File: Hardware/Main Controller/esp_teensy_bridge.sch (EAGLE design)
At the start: 4 parts, among them IC1 BQ79600PWRQ1

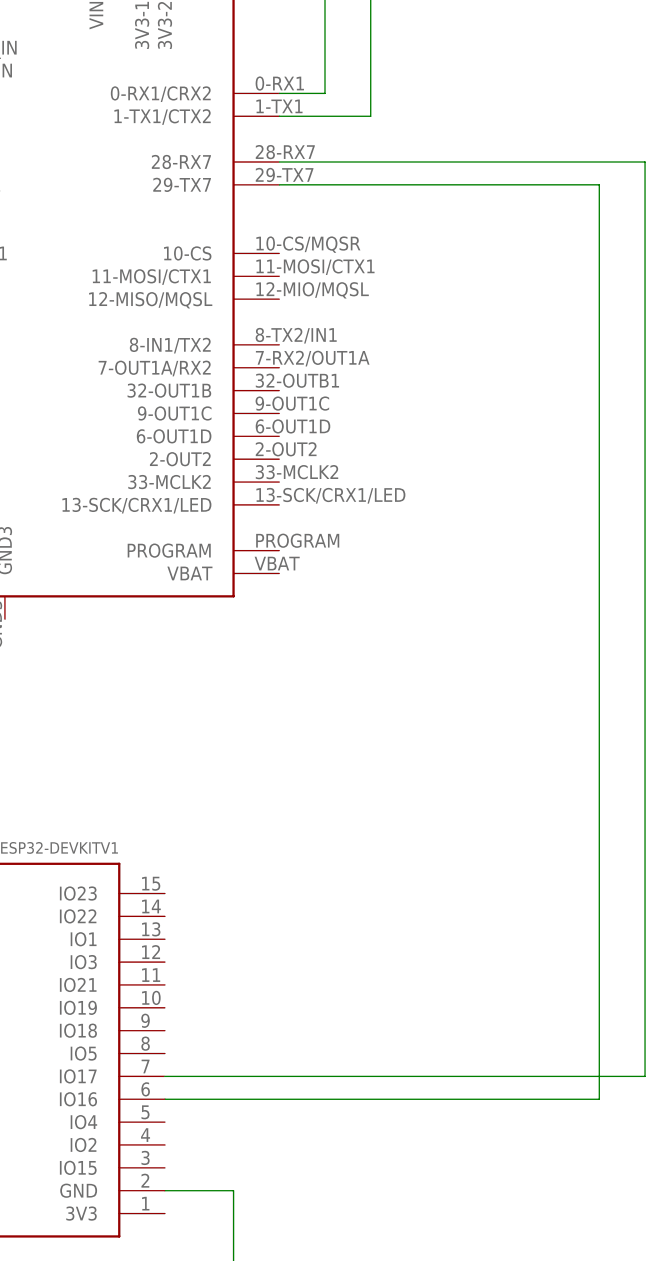
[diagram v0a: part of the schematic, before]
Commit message: Update esp_teensy_bridge.sch
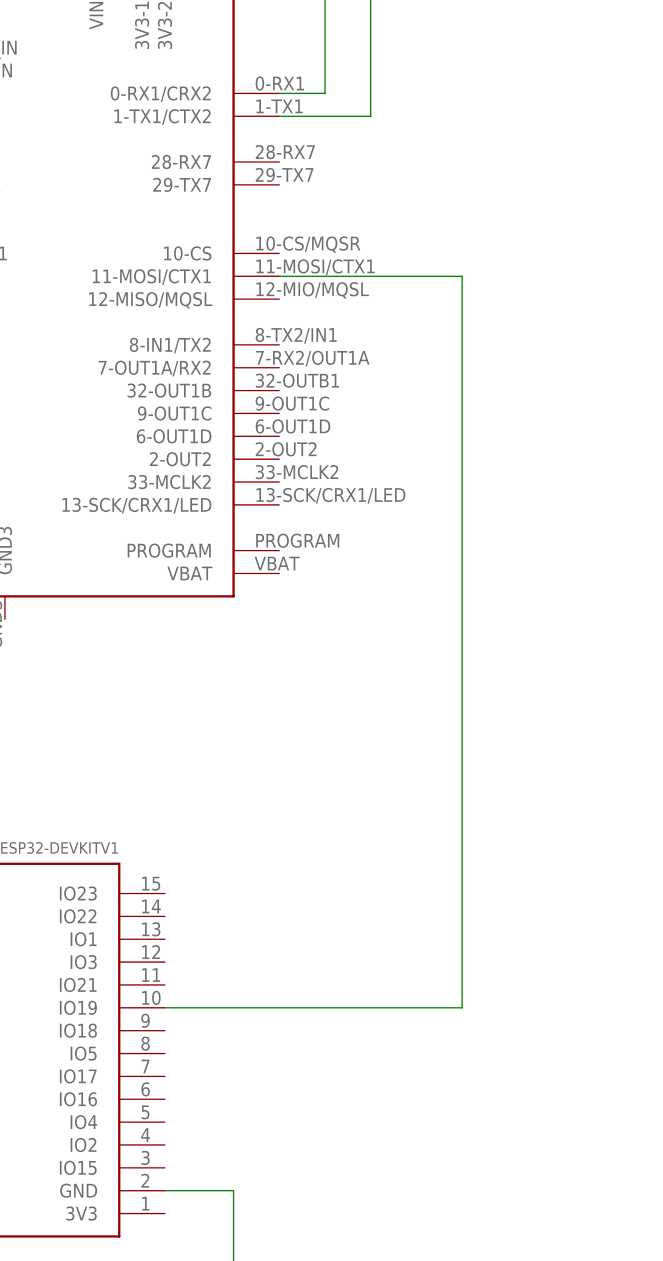
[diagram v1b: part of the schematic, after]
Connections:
- removed net N$8: U$1.29-TX7, U$2.IO16
- net N$2: now also U$1.11-MOSI/CTX1, U$2.IO19; no longer U$1.28-RX7, U$2.IO17
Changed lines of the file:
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@@
-</segment>
-</net>
-<net name="N$2" class="0">
-<segment>
-<wire x1="134.62" y1="-17.78" x2="134.62" y2="83.82" width="0.1524" layer="91"/>
-<pinref part="U$1" gate="G$1" pin="28-RX7"/>
-<wire x1="134.62" y1="83.82" x2="93.98" y2="83.82" width="0.1524" layer="91"/>
-<pinref part="U$2" gate="G$1" pin="IO17"/>
-<wire x1="81.28" y1="-17.78" x2="134.62" y2="-17.78" width="0.1524" layer="91"/>
-</segment>
-</net>
-<net name="N$8" class="0">
-<segment>
-<pinref part="U$1" gate="G$1" pin="29-TX7"/>
-<wire x1="93.98" y1="81.28" x2="129.54" y2="81.28" width="0.1524" layer="91"/>
-<pinref part="U$2" gate="G$1" pin="IO16"/>
-<wire x1="81.28" y1="-20.32" x2="129.54" y2="-20.32" width="0.1524" layer="91"/>
-<wire x1="129.54" y1="-20.32" x2="129.54" y2="81.28" width="0.1524" layer="91"/>
 </segment>
 </net>
@@
 </segment>
 </net>
+<net name="N$2" class="0">
+<segment>
+<pinref part="U$1" gate="G$1" pin="11-MOSI/CTX1"/>
+<wire x1="93.98" y1="71.12" x2="114.3" y2="71.12" width="0.1524" layer="91"/>
+<wire x1="114.3" y1="71.12" x2="114.3" y2="-10.16" width="0.1524" layer="91"/>
+<pinref part="U$2" gate="G$1" pin="IO19"/>
+<wire x1="114.3" y1="-10.16" x2="81.28" y2="-10.16" width="0.1524" layer="91"/>
+</segment>
+</net>

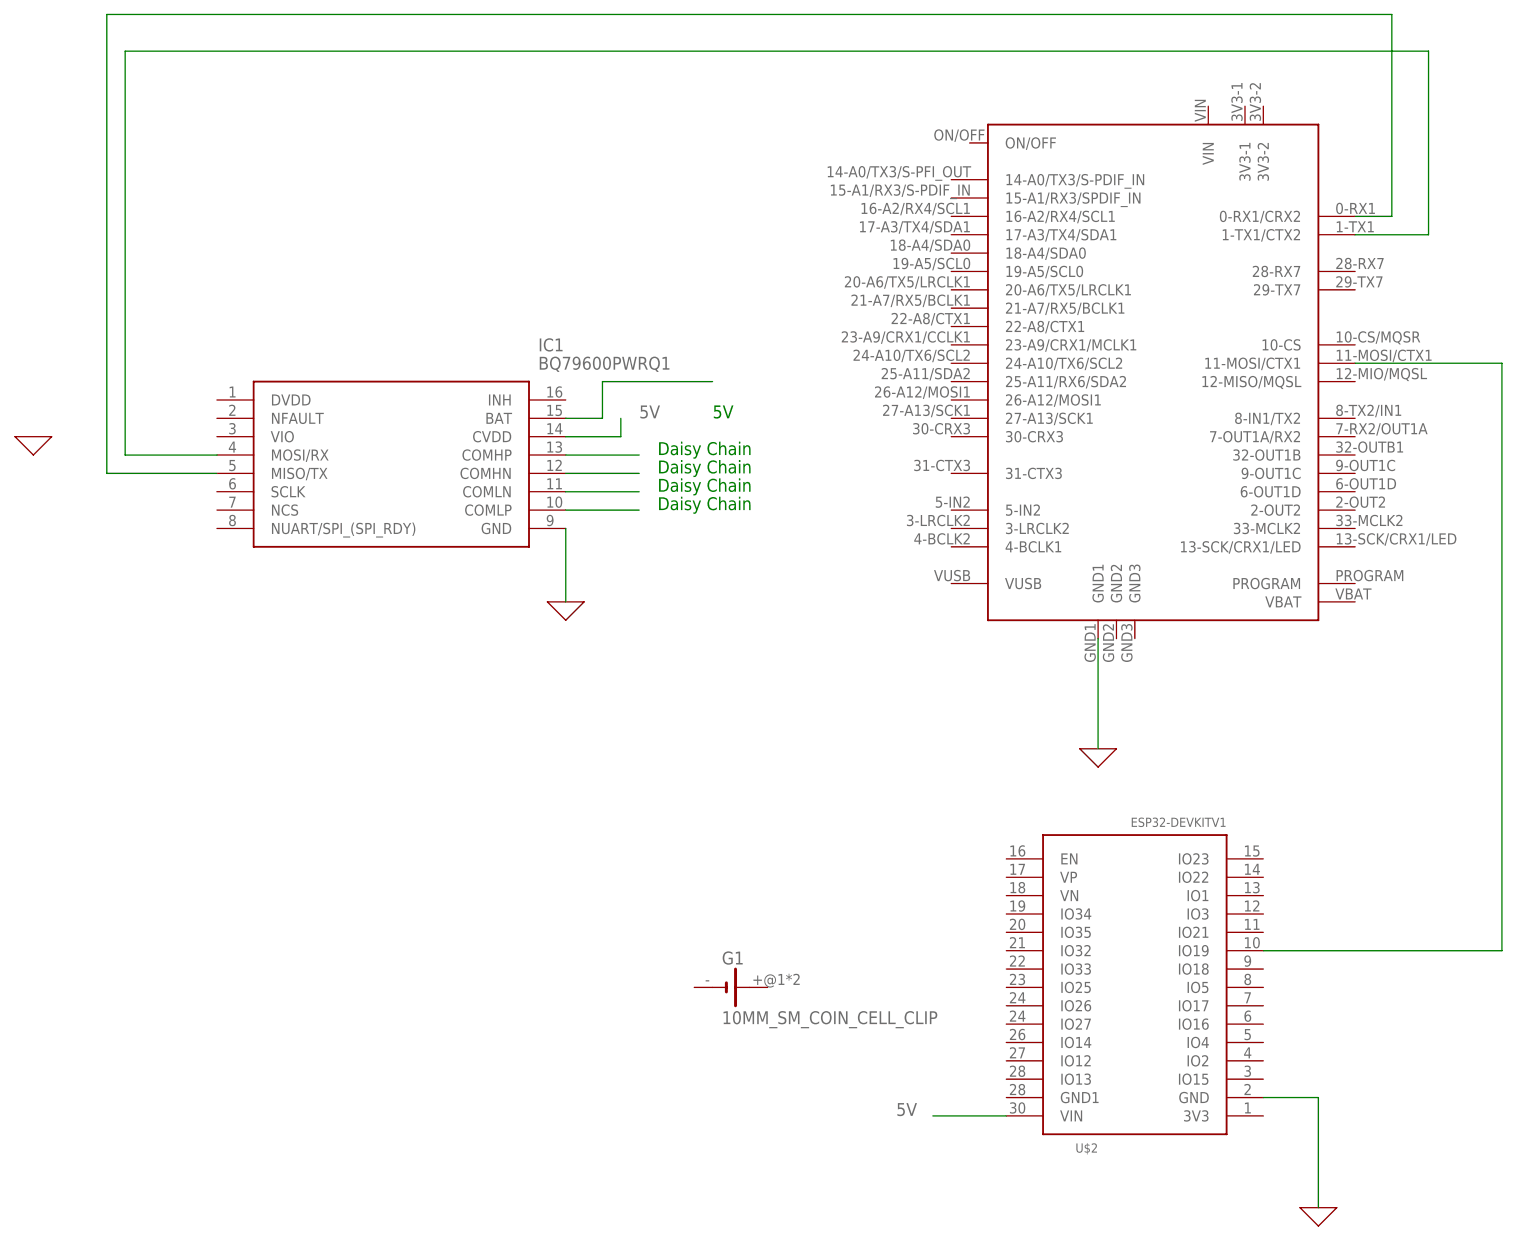
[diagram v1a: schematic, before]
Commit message: Update esp_teensy_bridge.sch
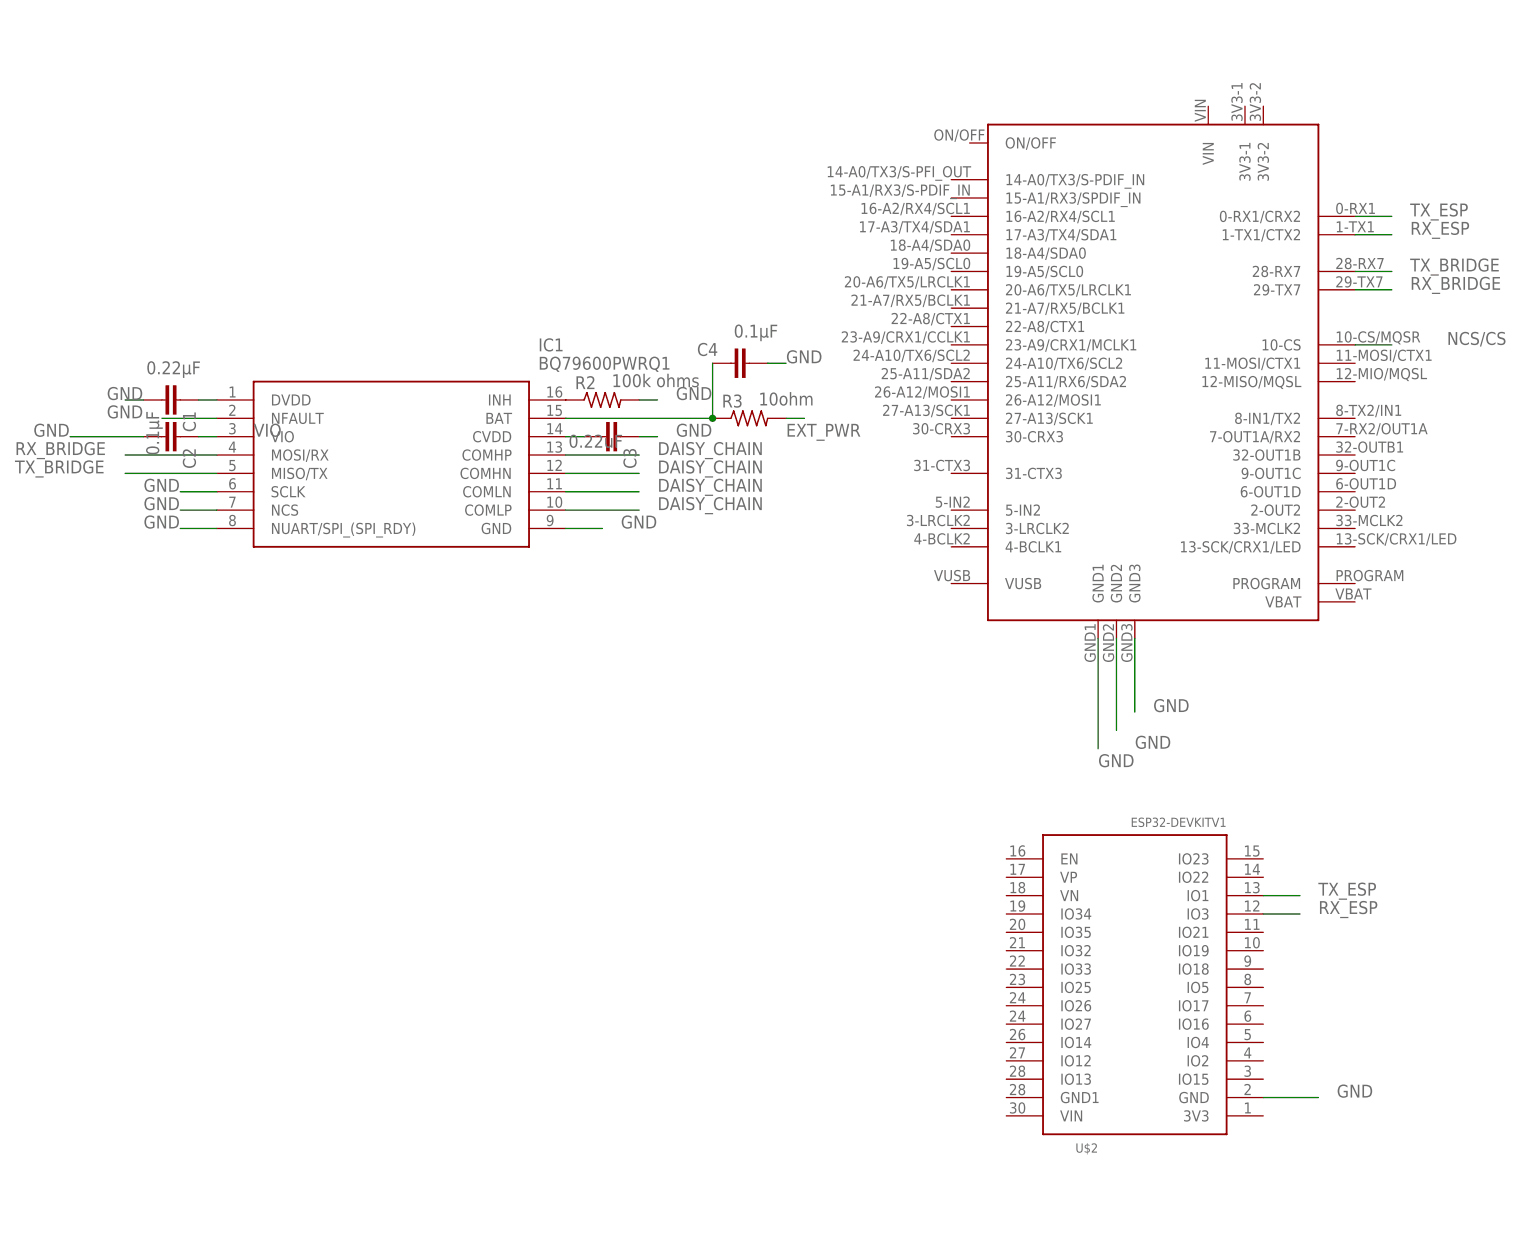
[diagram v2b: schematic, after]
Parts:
- removed G1: 10MM_SM_COIN_CELL_CLIP, battery:10MM_SM_COIN_CELL_CLIP
- added C1: 0.22μF, capacitor-wima:C2,5-3
- added C2, C4: 0.1μF, capacitor-wima:C2,5-3
- added C3: 0.22uF, capacitor-wima:C2.5/2
- added R2: 100k ohms, rcl:R-US_0204/7
- added R3: 10ohm, rcl:R-US_0204/7
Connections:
- removed net 0: IC1.GND, U$1.GND1, U$2.GND
- removed net 5V: IC1.CVDD, U$2.VIN
- removed net N$10: IC1.BAT
- removed net N$2: U$1.11-MOSI/CTX1, U$2.IO19
- removed net N$6: IC1.COMHP
- removed net N$7: IC1.MOSI/RX, U$1.1-TX1/CTX2
- new net DAISY_CHAIN: IC1.COMHN, IC1.COMHP, IC1.COMLN, IC1.COMLP
- new net EXT_PWR: R3.2
- new net GND: C1.2, C2.2, C3.1, C4.1, IC1.GND, IC1.NCS, IC1.NFAULT, IC1.NUART/SPI_(SPI_RDY), IC1.SCLK, R2.2, U$1.GND1, U$1.GND2, U$1.GND3, U$2.GND
- new net NCS/CS: U$1.10-CS
- new net RX_BRIDGE: IC1.MOSI/RX, U$1.29-TX7
- new net RX_ESP: U$1.1-TX1/CTX2, U$2.IO3
- new net TX_BRIDGE: IC1.MISO/TX, U$1.28-RX7
- new net TX_ESP: U$1.0-RX1/CRX2, U$2.IO1
- new net VIO: C2.1, IC1.VIO
- net N$1: now also C1.1, IC1.DVDD; no longer IC1.MISO/TX, U$1.0-RX1/CRX2
- net N$3: now also C3.2, IC1.CVDD; no longer IC1.COMLP
- net N$4: now also IC1.INH, R2.1; no longer IC1.COMLN
- net N$5: now also C4.2, IC1.BAT, R3.1; no longer IC1.COMHN
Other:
- note removed: "5V"
- note removed: "Daisy Chain"
